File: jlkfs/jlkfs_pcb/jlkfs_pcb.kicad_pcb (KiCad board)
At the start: 2 copper layers, 133.4 x 118.4 mm, 38 parts, among them J0 Conn_01x02_Socket, SW0 SWITCH, SW1 SWITCH, SW10 SWITCH, SW11 SWITCH, SW12 SWITCH, SW13 SWITCH, SW14 SWITCH, SW15 SWITCH, SW16 SWITCH, SW17 SWITCH, SW18 SWITCH, SW19 SWITCH, SW2 SWITCH, SW20 SWITCH, SW21 SWITCH, SW22 SWITCH, SW23 SWITCH, SW24 SWITCH, SW25 SWITCH, SW26 SWITCH, SW27 SWITCH, SW28 SWITCH, SW29 SWITCH, SW3 SWITCH, SW4 SWITCH, SW5 SWITCH, SW6 SWITCH, SW7 SWITCH, SW8 SWITCH, SW9 SWITCH, U0 NICE!

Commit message: Routed jlkfs.
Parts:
- U0: moved to B.Cu
- moved PWR0 48.3 mm to (161.9, 20.3)
- moved SW16 48.3 mm to (161.9, 38.7)
- moved SW17 48.3 mm to (161.9, 57.8)
- moved SW18 48.3 mm to (161.9, 76.8)
- moved SW19 48.3 mm to (161.9, 95.9)
- moved SW20 48.3 mm to (161.9, 114.9)
- moved H1 48.3 mm to (104.8, 36.4)
- moved RST0 48.3 mm to (104.8, 29.9)
- moved SW3 48.3 mm to (104.8, 47.6)
- moved SW4 48.3 mm to (104.8, 66.7)
- moved SW5 48.3 mm to (104.8, 85.7)
- moved SW6 48.3 mm to (104.8, 104.8)
- moved H0 48.3 mm to (192.2, 41.1)
- moved H2 48.3 mm to (95.2, 114.3)
- moved H3 48.3 mm to (190.5, 134.0)
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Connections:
- SW0 pad 1: Net-(SW0-Pad1) -> /COL6
- SW0 pad 3: Net-(SW0-K) -> /ROW1
- SW1 pad 1: Net-(SW0-Pad1) -> /COL6
- SW1 pad 3: Net-(SW1-K) -> /ROW2
- SW10 pad 1: Net-(SW10-Pad1) -> /COL4
- SW10 pad 3: Net-(SW10-K) -> /ROW3
- SW11 pad 1: Net-(SW11-Pad1) -> /COL3
- SW11 pad 3: Net-(SW11-K) -> /ROW0
- SW12 pad 1: Net-(SW11-Pad1) -> /COL3
- SW12 pad 3: Net-(SW0-K) -> /ROW1
- SW13 pad 1: Net-(SW11-Pad1) -> /COL3
- SW13 pad 3: Net-(SW1-K) -> /ROW2
- SW14 pad 1: Net-(SW11-Pad1) -> /COL3
- SW14 pad 3: Net-(SW10-K) -> /ROW3
- SW15 pad 1: Net-(SW11-Pad1) -> /COL3
- SW15 pad 3: Net-(SW15-K) -> /ROW4
- SW16 pad 1: Net-(SW16-Pad1) -> /COL2
- SW16 pad 3: Net-(SW11-K) -> /ROW0
- SW17 pad 1: Net-(SW16-Pad1) -> /COL2
- SW17 pad 3: Net-(SW0-K) -> /ROW1
- SW18 pad 1: Net-(SW16-Pad1) -> /COL2
- SW18 pad 3: Net-(SW1-K) -> /ROW2
- SW19 pad 1: Net-(SW16-Pad1) -> /COL2
- SW19 pad 3: Net-(SW10-K) -> /ROW3
- SW2 pad 1: Net-(SW0-Pad1) -> /COL6
- SW2 pad 3: Net-(SW10-K) -> /ROW3
- SW20 pad 1: Net-(SW16-Pad1) -> /COL2
- SW20 pad 3: Net-(SW15-K) -> /ROW4
- SW21 pad 1: Net-(SW21-Pad1) -> /COL1
- SW21 pad 3: Net-(SW11-K) -> /ROW0
- SW22 pad 1: Net-(SW21-Pad1) -> /COL1
- SW22 pad 3: Net-(SW0-K) -> /ROW1
- SW23 pad 1: Net-(SW21-Pad1) -> /COL1
- SW23 pad 3: Net-(SW1-K) -> /ROW2
- SW24 pad 1: Net-(SW21-Pad1) -> /COL1
- SW24 pad 3: Net-(SW10-K) -> /ROW3
- SW25 pad 1: Net-(SW21-Pad1) -> /COL1
- SW25 pad 3: Net-(SW15-K) -> /ROW4
- SW26 pad 1: Net-(SW26-Pad1) -> /COL0
- SW26 pad 3: Net-(SW0-K) -> /ROW1
- SW27 pad 1: Net-(SW26-Pad1) -> /COL0
- SW27 pad 3: Net-(SW1-K) -> /ROW2
- SW28 pad 1: Net-(SW26-Pad1) -> /COL0
- SW28 pad 3: Net-(SW10-K) -> /ROW3
- SW29 pad 1: Net-(SW26-Pad1) -> /COL0
- SW29 pad 3: Net-(SW15-K) -> /ROW4
- SW3 pad 1: Net-(SW3-Pad1) -> /COL5
- SW3 pad 3: Net-(SW11-K) -> /ROW0
- SW4 pad 1: Net-(SW3-Pad1) -> /COL5
- SW4 pad 3: Net-(SW0-K) -> /ROW1
- SW5 pad 1: Net-(SW3-Pad1) -> /COL5
- SW5 pad 3: Net-(SW1-K) -> /ROW2
- SW6 pad 1: Net-(SW3-Pad1) -> /COL5
- SW6 pad 3: Net-(SW10-K) -> /ROW3
- SW7 pad 1: Net-(SW10-Pad1) -> /COL4
- SW7 pad 3: Net-(SW11-K) -> /ROW0
- SW8 pad 1: Net-(SW10-Pad1) -> /COL4
- SW8 pad 3: Net-(SW0-K) -> /ROW1
- SW9 pad 1: Net-(SW10-Pad1) -> /COL4
- SW9 pad 3: Net-(SW1-K) -> /ROW2
- U0 pad 1: /KEY0 -> /COL0
- U0 pad 10: /KEY10 -> unconnected-(U0-E6-Pad10)
- U0 pad 11: /KEY13 -> /ROW3
- U0 pad 12: /KEY2 -> /ROW2
- U0 pad 13: /KEY16 -> /COL6
- U0 pad 14: /KEY15 -> /ROW1
- U0 pad 15: /KEY14 -> /ROW4
- U0 pad 16: /KEY11 -> unconnected-(U0-B1-Pad16)
- U0 pad 17: /KEY8 -> unconnected-(U0-F7-Pad17)
- U0 pad 18: /KEY5 -> unconnected-(U0-F6-Pad18)
- U0 pad 2: /KEY3 -> /COL1
- U0 pad 20: /KEY6 -> unconnected-(U0-F4-Pad20)
- U0 pad 5: /KEY9 -> /COL2
- U0 pad 6: /KEY12 -> /COL3
- U0 pad 7: /KEY1 -> /COL4
- U0 pad 8: /KEY4 -> /COL5
- U0 pad 9: /KEY7 -> /ROW0
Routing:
- net /ROW3: track 0.00 -> 226.0 mm, vias 0 -> 7
- net /COL0: track 0.00 -> 212.8 mm, vias 0 -> 4
- net /ROW4: track 0.00 -> 207.0 mm, vias 0 -> 4
- net /ROW2: track 0.00 -> 204.1 mm, vias 0 -> 7
- net /COL1: track 0.00 -> 198.4 mm, vias 0 -> 5
- net /ROW1: track 0.00 -> 196.3 mm, vias 0 -> 7
- net /COL2: track 0.00 -> 175.0 mm, vias 0 -> 5
- net /COL3: track 0.00 -> 147.2 mm, vias 0 -> 5
- net /ROW0: track 0.00 -> 117.9 mm, vias 0 -> 5
- net /COL4: track 0.00 -> 101.6 mm, vias 0 -> 4
- net /RAW: track 0.00 -> 85.0 mm
- net /COL5: track 0.00 -> 80.4 mm, vias 0 -> 4
- net /COL6: track 0.00 -> 61.9 mm, vias 0 -> 3
- net /RST: track 0.00 -> 26.3 mm
- net /B+: track 0.00 -> 25.7 mm
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- added copper zone on B.Cu, net GND
- added copper zone on F.Cu, net GND

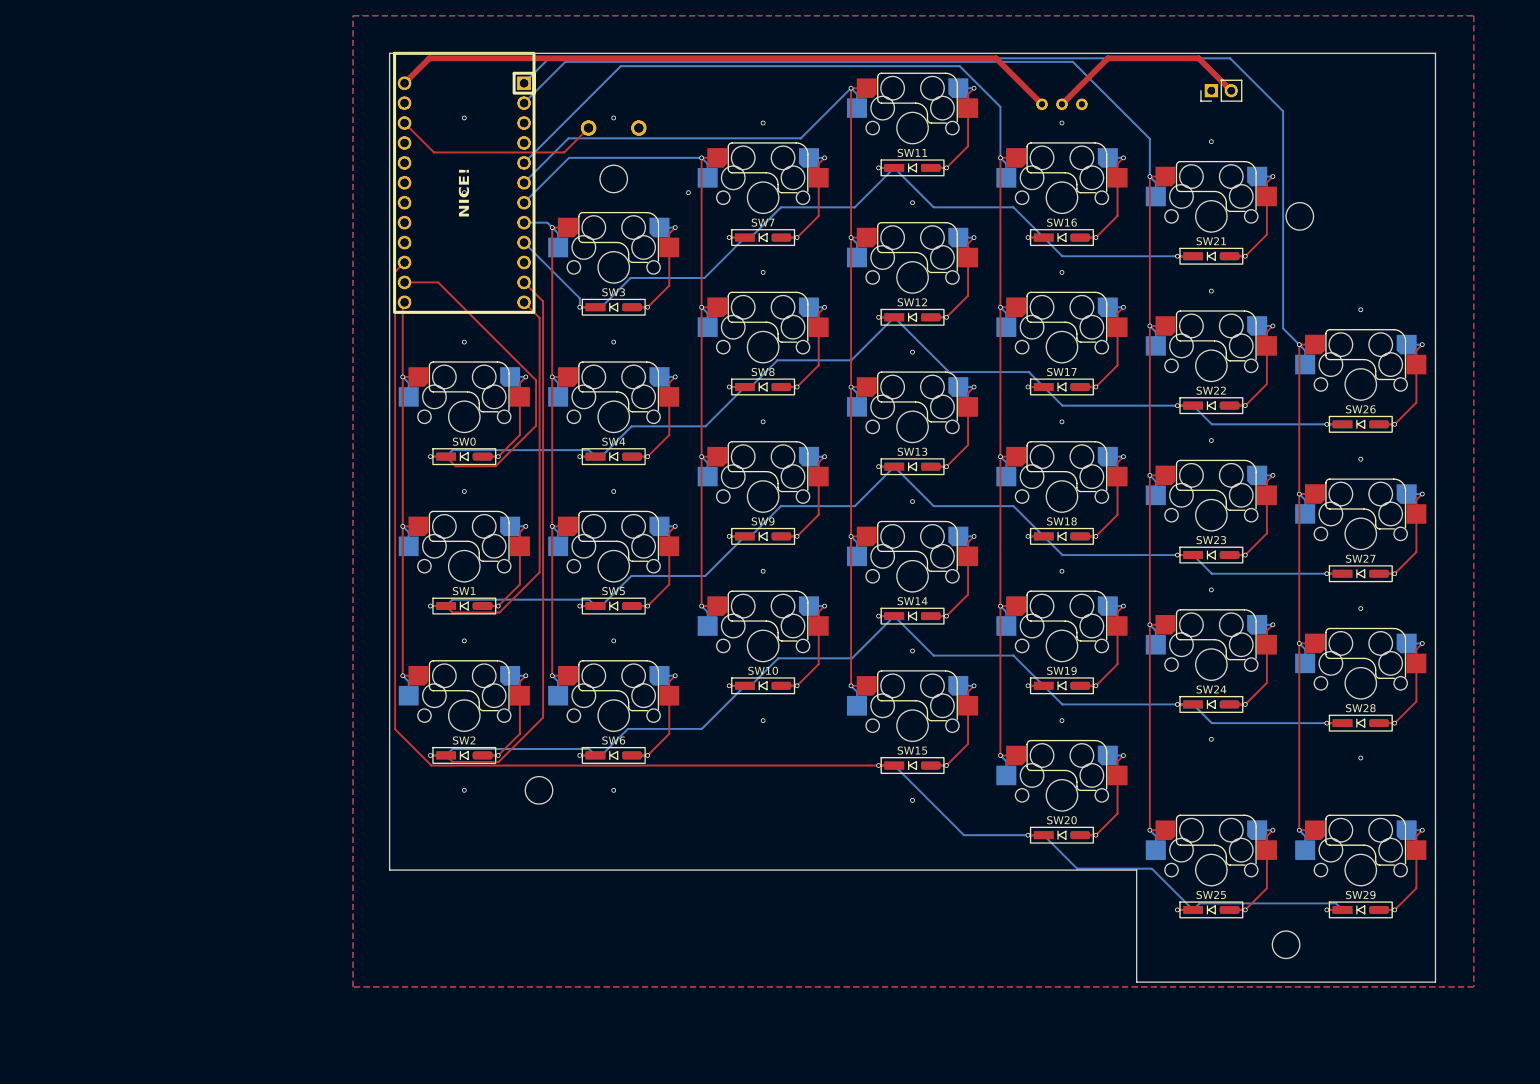
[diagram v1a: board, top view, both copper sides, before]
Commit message: Moved the outside pinky row down slightly.
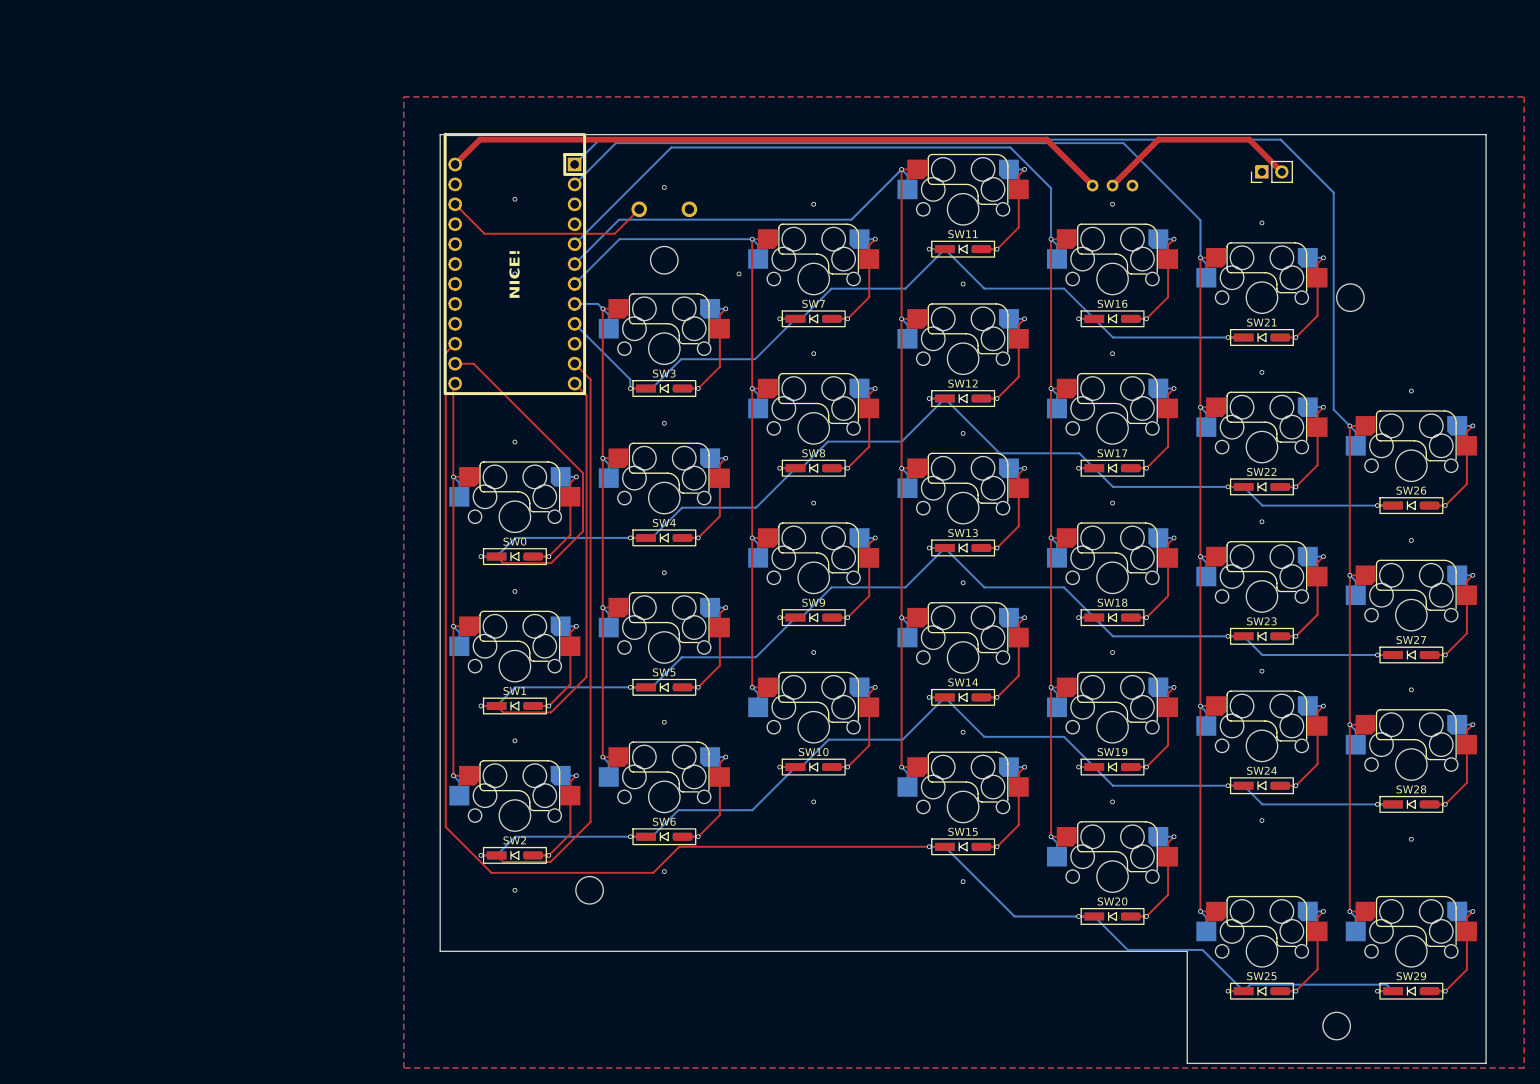
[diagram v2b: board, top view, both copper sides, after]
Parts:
- moved H2 14.3 mm to (101.7, 127.0)
- moved SW0 14.3 mm to (92.2, 79.4)
- moved SW1 14.3 mm to (92.2, 98.5)
- moved SW2 14.3 mm to (92.2, 117.5)
- moved SW22 12.2 mm to (187.4, 70.5)
- moved J0 12.2 mm to (187.4, 35.5)
- moved SW21 12.2 mm to (187.4, 51.5)
- moved SW23 12.2 mm to (187.4, 89.6)
- moved SW24 12.2 mm to (187.4, 108.6)
- moved SW25 12.2 mm to (187.4, 134.8)
- moved SW10 12.2 mm to (130.3, 106.3)
- moved SW7 12.2 mm to (130.3, 49.1)
- moved SW9 12.2 mm to (130.3, 87.2)
- moved U0 12.2 mm to (92.2, 30.7)
- moved SW8 12.2 mm to (130.3, 68.2)
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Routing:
- net /ROW3: track 226.0 -> 228.5 mm
- net /COL6: track 61.9 -> 64.3 mm
- net /ROW2: track 204.1 -> 206.5 mm
- net /ROW4: track 207.0 -> 209.0 mm
- net /ROW1: track 196.3 -> 197.3 mm
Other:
- board size 133.4 x 118.4 mm -> 133.3 x 118.4 mm
